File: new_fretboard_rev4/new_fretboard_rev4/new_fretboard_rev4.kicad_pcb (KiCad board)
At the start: 4 copper layers, 585 x 79 mm, 45 parts, among them CN1 Header 1x6, CN2 Header 1x6, J1 JMP, J2 JMP, J4 JMP, J8 JMP, U1 LX3302AQPW_TSSOP-14, U2 LX3302AQPW_TSSOP-14

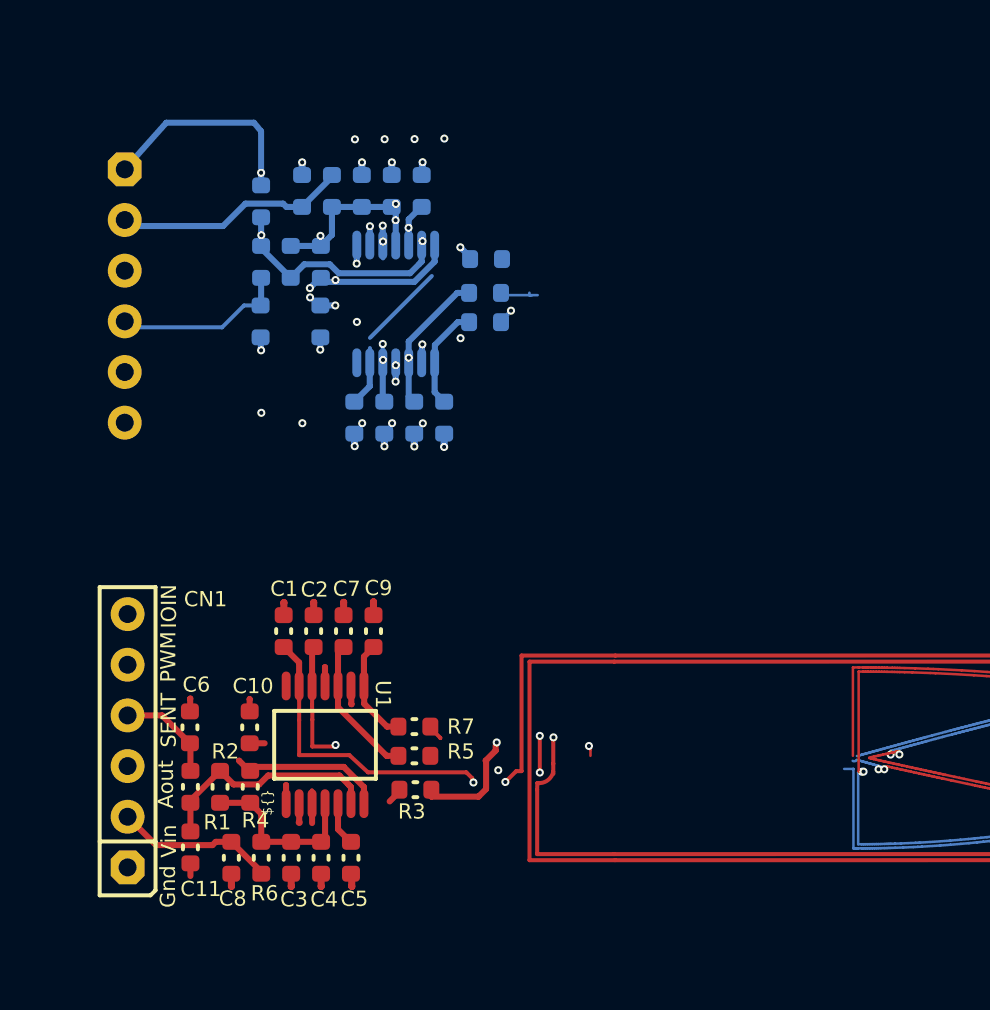
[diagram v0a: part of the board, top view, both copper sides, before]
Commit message: sinA and cosA correct, and sinB correct
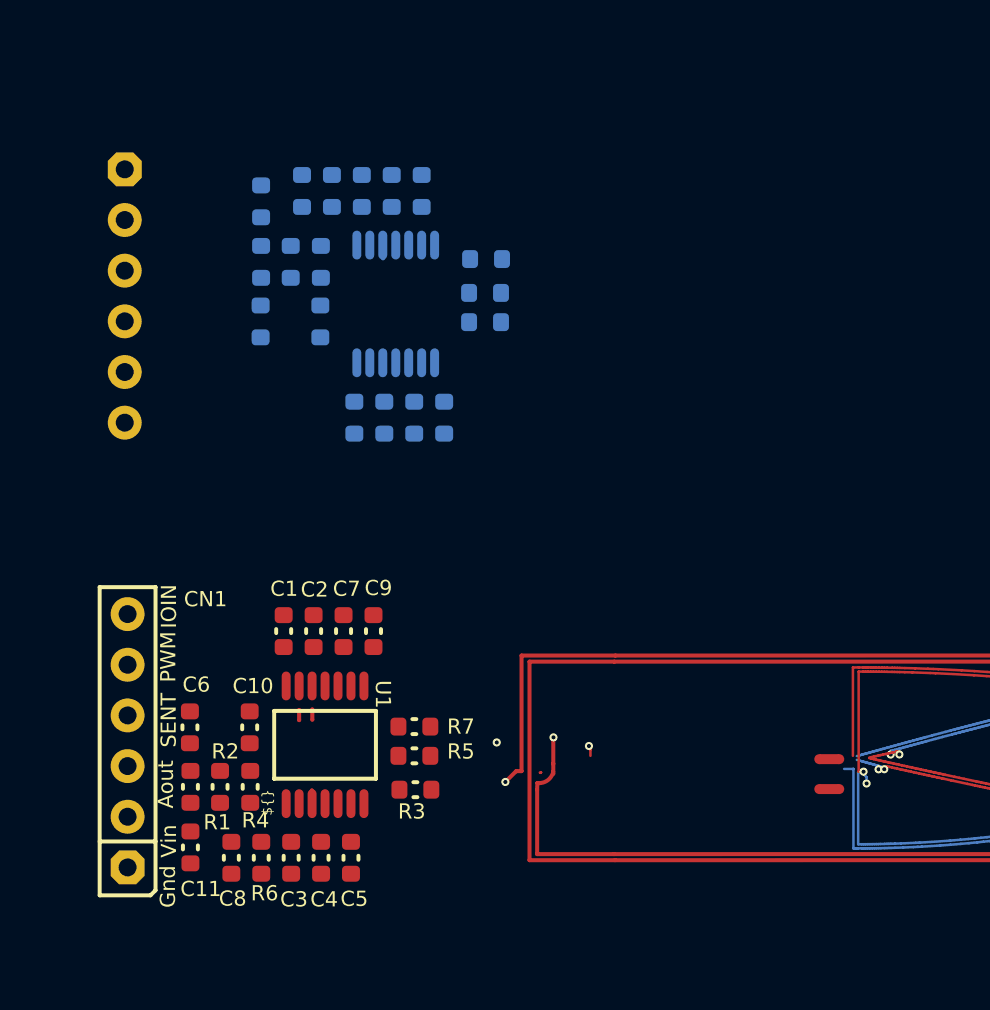
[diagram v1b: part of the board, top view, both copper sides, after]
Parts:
- added L3: PCB L, NetTie:NetTie-2_SMD_Pad0.5mm, F.Cu at (45.9, 131.5)
- added L4: PCB L, NetTie:NetTie-2_SMD_Pad0.5mm, F.Cu at (45.9, 133.0)
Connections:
- net /COS_B_ renamed /OSC_CCW_A
- net /OSC1B renamed /OSC_CW_A
- J4 pad 2: /CL1B -> /SIN_A
- J8 pad 2: /CL1B -> /SIN_B (x2)
- R13 pad 2: /SIN_B -> Net-(J7-Pad1)
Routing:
- net /COS_A: track 0.00 -> 4225.7 mm, vias 0 -> 39
- net /OSC_CCW_A: track 4308.6 -> 2180.6 mm, vias 44 -> 40
- net /COS_B: track 2104.1 -> 0.00 mm, vias 1 -> 0
- net /SIN_A: track 0.00 -> 2083.0 mm, vias 0 -> 38
- net /SIN_A_ch1: track 2074.2 -> 0.00 mm
- net GND1: track 54.7 -> 26.8 mm, vias 23 -> 0
- net Net-(U1-IO2): track 23.5 -> 0.00 mm
- net /VIN: track 19.8 -> 0.00 mm
- net VIN1: track 26.9 -> 7.91 mm, vias 5 -> 0
- net /CL12: track 14.4 -> 0.00 mm, vias 1 -> 0
- net Net-(L1-Pad2): track 13.2 -> 0.00 mm, vias 1 -> 0
- net /OSC_CW_A: track 11.2 -> 0.00 mm, vias 1 -> 0
- net /CL11: track 10.5 -> 0.00 mm
- net Net-(C12-Pad2): track 7.90 -> 0.00 mm
- net Net-(U1-IO1): track 15.7 -> 7.91 mm, vias 1 -> 0
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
